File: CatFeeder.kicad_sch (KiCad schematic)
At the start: 54 parts, among them J1 B2B-XH-A(LF)(SN), J10 B2B-XH-A(LF)(SN), J11 B2B-XH-A(LF)(SN), J12 B2B-XH-A(LF)(SN), J13 B2B-XH-A(LF)(SN), J2 B2B-XH-A(LF)(SN), J3 B3B-XH-A(LF)(SN), J4 Barrel_Jack, J5 B4B-XH-A(LF)(SN), J6 Conn_01x08_Female, J7 Conn_01x08_Female, J8 B2B-XH-A(LF)(SN), J9 B2B-XH-A(LF)(SN), Q1 Q_NPN_BEC, Q2 Q_NPN_BEC, U1 SN74LVC1T45DBV, U2 LM2586SX-ADJ/NOPB_1, U3 DRV8871DDA

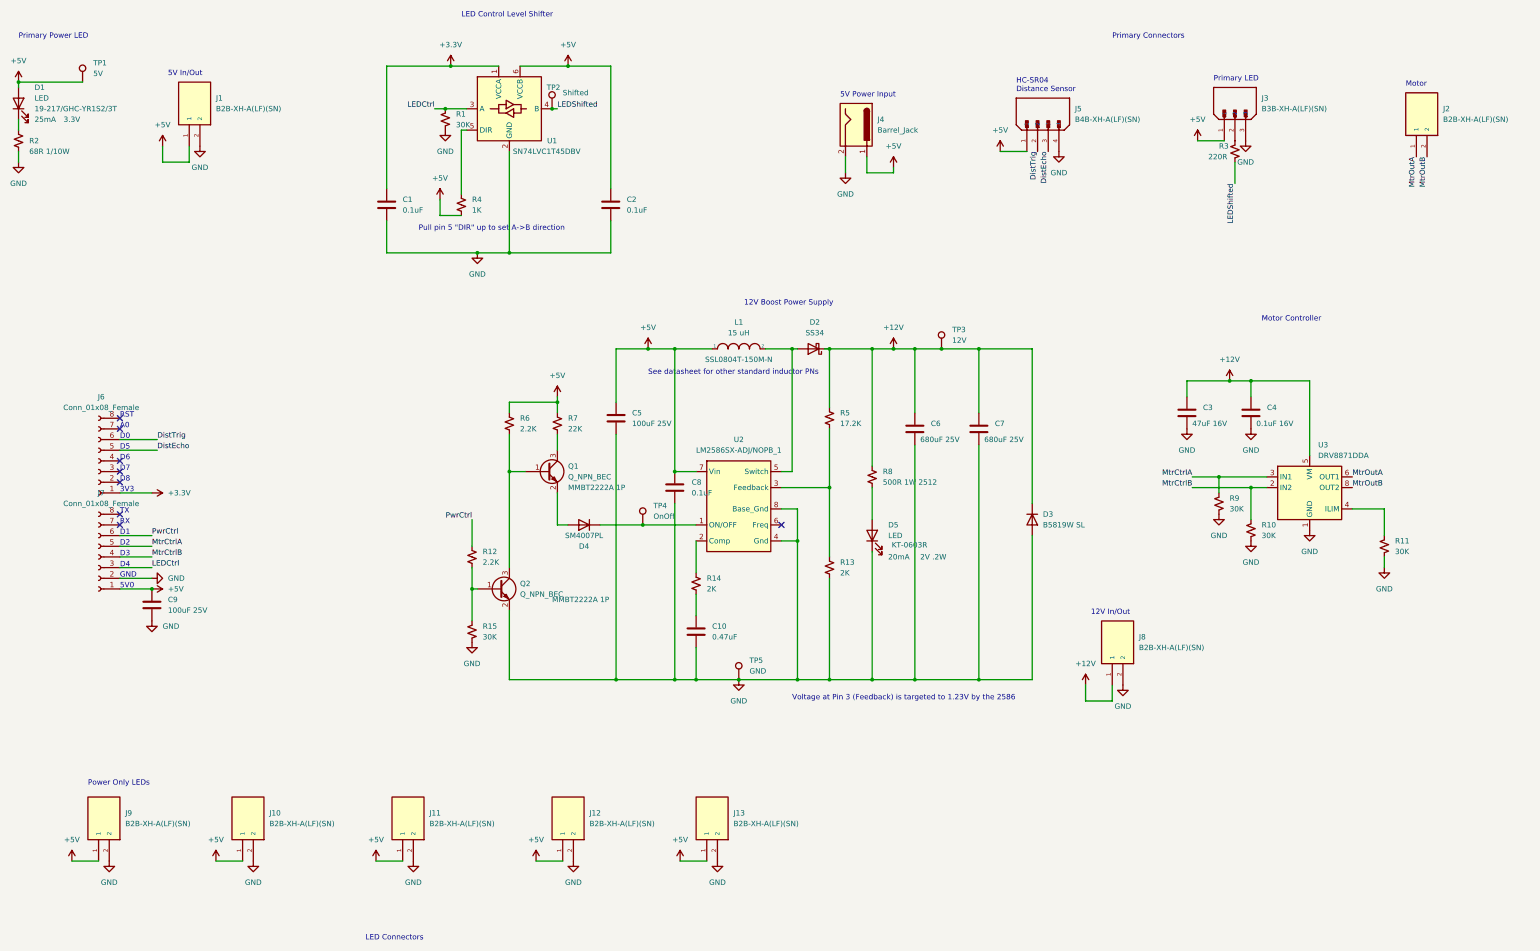
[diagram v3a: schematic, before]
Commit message: rounded corners, added polarity silkscreen, dimmed the main power LED, fixed polarized cap schematic symbols.
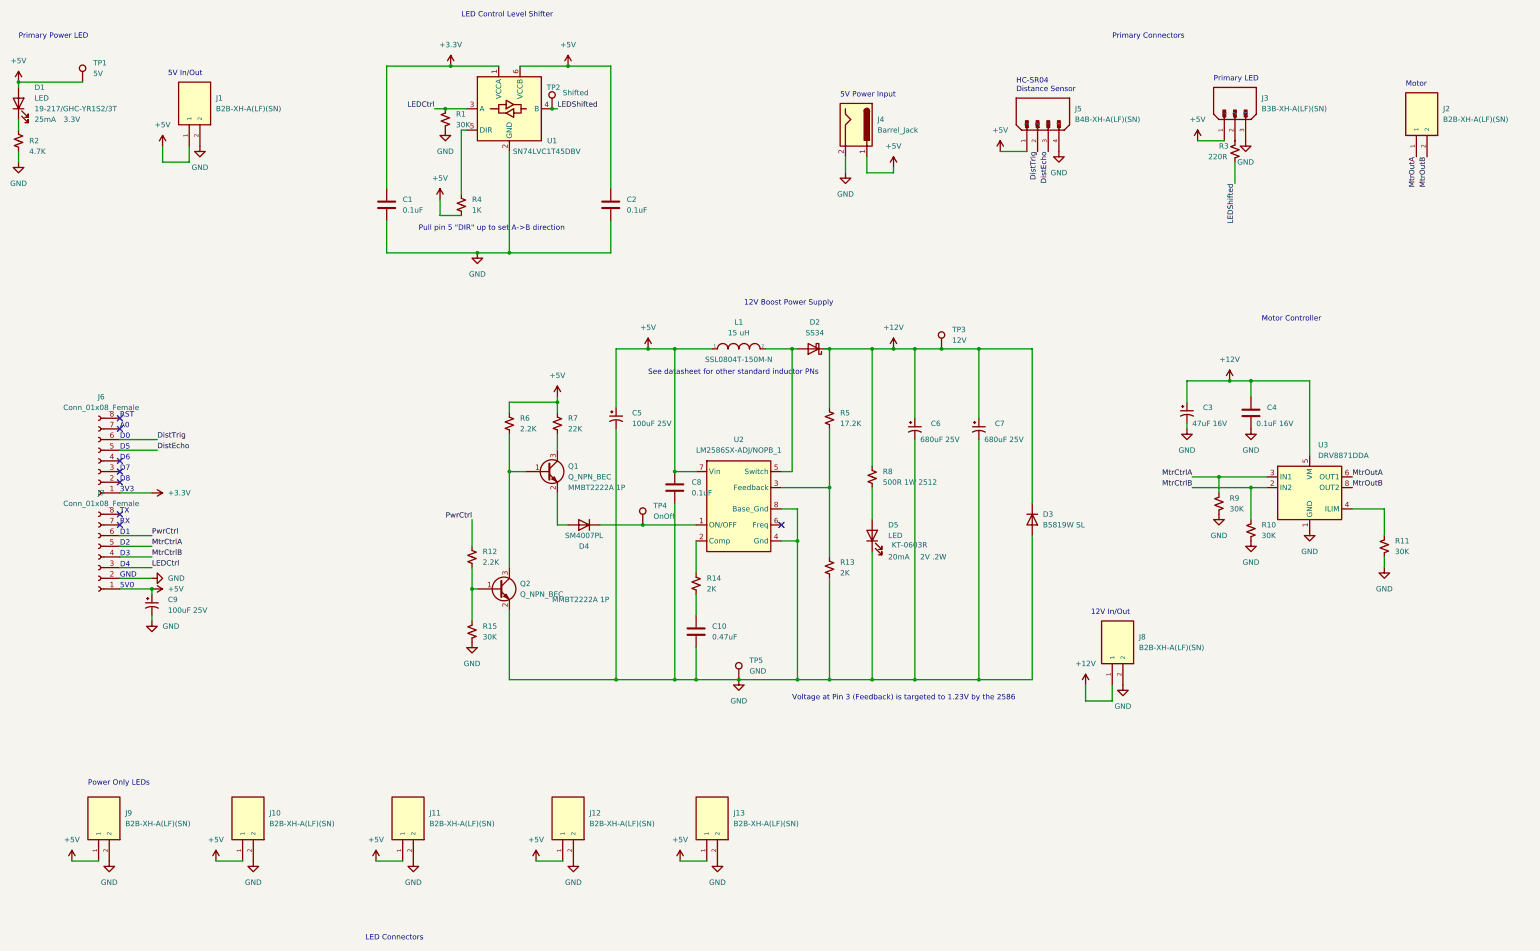
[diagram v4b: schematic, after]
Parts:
- C3, C5, C6, C7, C9: symbol Device:C -> Device:C_Polarized_Small_US
- R2: value 68R 1/10W -> 4.7K; footprint Resistor_SMD:R_0603_1608Metric -> Resistor_SMD:R_0805_2012Metric; PN 0603WAF680JT5E -> 0805W8F4701T5E
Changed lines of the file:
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@@
   (junction (at 233.68 102.87) (diameter 0) (color 0 0 0 0)
   )
+  (junction (at 72.39 160.02) (diameter 0) (color 0 0 0 0)
+  )
   (junction (at 189.23 144.78) (diameter 0) (color 0 0 0 0)
   )
@@
   (junction (at 212.09 181.61) (diameter 0) (color 0 0 0 0)
   )
-  (junction (at 72.39 160.02) (diameter 0) (color 0 0 0 0)
-  )
   (junction (at 233.68 181.61) (diameter 0) (color 0 0 0 0)
   )
@@
     (stroke (width 0) (type default) (color 0 0 0 0))
   )
-  (wire (pts (xy 254 125.73) (xy 254 181.61))
+  (wire (pts (xy 254 124.46) (xy 254 181.61))
     (stroke (width 0) (type default) (color 0 0 0 0))
   )
@@
     (stroke (width 0) (type default) (color 0 0 0 0))
   )
-  (wire (pts (xy 182.88 123.19) (xy 182.88 181.61))
+  (wire (pts (xy 182.88 121.92) (xy 182.88 181.61))
     (stroke (width 0) (type default) (color 0 0 0 0))
   )
@@
     (stroke (width 0) (type default) (color 0 0 0 0))
   )
-  (wire (pts (xy 269.24 125.73) (xy 269.24 181.61))
+  (wire (pts (xy 269.24 124.46) (xy 269.24 181.61))
     (stroke (width 0) (type default) (color 0 0 0 0))
   )
@@
     (stroke (width 0) (type default) (color 0 0 0 0))
   )
-  (wire (pts (xy 318.77 110.49) (xy 318.77 114.3))
+  (wire (pts (xy 318.77 110.49) (xy 318.77 115.57))
     (stroke (width 0) (type default) (color 0 0 0 0))
   )
@@
     (stroke (width 0) (type default) (color 0 0 0 0))
   )
-  (wire (pts (xy 182.88 102.87) (xy 182.88 115.57))
+  (wire (pts (xy 182.88 102.87) (xy 182.88 116.84))
     (stroke (width 0) (type default) (color 0 0 0 0))
   )
@@
     (stroke (width 0) (type default) (color 0 0 0 0))
   )
-  (wire (pts (xy 254 118.11) (xy 254 102.87))
+  (wire (pts (xy 254 102.87) (xy 254 119.38))
     (stroke (width 0) (type default) (color 0 0 0 0))
   )
@@
     (stroke (width 0) (type default) (color 0 0 0 0))
   )
-  (wire (pts (xy 269.24 118.11) (xy 269.24 102.87))
+  (wire (pts (xy 269.24 102.87) (xy 269.24 119.38))
     (stroke (width 0) (type default) (color 0 0 0 0))
   )
@@
     (stroke (width 0) (type default) (color 0 0 0 0))
   )
+  (wire (pts (xy 72.39 160.02) (xy 72.39 161.29))
+    (stroke (width 0) (type default) (color 0 0 0 0))
+  )
   (wire (pts (xy 198.12 224.79) (xy 204.47 224.79))
     (stroke (width 0) (type default) (color 0 0 0 0))
@@
     (stroke (width 0) (type default) (color 0 0 0 0))
   )
+  (wire (pts (xy 72.39 166.37) (xy 72.39 167.64))
+    (stroke (width 0) (type default) (color 0 0 0 0))
+  )
   (wire (pts (xy 128.27 35.56) (xy 128.27 64.77))
     (stroke (width 0) (type default) (color 0 0 0 0))
@@
     (stroke (width 0) (type default) (color 0 0 0 0))
   )
+  (wire (pts (xy 318.77 120.65) (xy 318.77 121.92))
+    (stroke (width 0) (type default) (color 0 0 0 0))
+  )
   (wire (pts (xy 157.48 80.01) (xy 181.61 80.01))
     (stroke (width 0) (type default) (color 0 0 0 0))
@@
     (pin "6")
   )
-  (symbol (lib_id "Device:C") (at 72.39 163.83 0) (unit 1)
+  (symbol (lib_id "Device:C_Polarized_Small_US") (at 72.39 163.83 0) (unit 1)
     (in_bom yes) (on_board yes) (fields_autoplaced)
     (property "Reference" "C9" (id 0) (at 76.2 162.5599 0)
@@
       (effects (font (size 1.27 1.27)) (justify left))
     )
-    (property "Footprint" "Capacitor_THT:CP_Radial_D8.0mm_P3.50mm" (id 2) (at 73.3552 167.64 0)
+    (property "Footprint" "Capacitor_THT:CP_Radial_D8.0mm_P3.50mm" (id 2) (at 72.39 163.83 0)
       (effects (font (size 1.27 1.27)) hide)
     )
@@
     (pin "2")
   )
-  (symbol (lib_id "Device:C") (at 182.88 119.38 0) (unit 1)
+  (symbol (lib_id "Device:C_Polarized_Small_US") (at 182.88 119.38 0) (unit 1)
     (in_bom yes) (on_board yes) (fields_autoplaced)
     (property "Reference" "C5" (id 0) (at 186.69 118.1099 0)
@@
       (effects (font (size 1.27 1.27)) (justify left))
     )
-    (property "Footprint" "Capacitor_THT:CP_Radial_D8.0mm_P3.50mm" (id 2) (at 183.8452 123.19 0)
+    (property "Footprint" "Capacitor_THT:CP_Radial_D8.0mm_P3.50mm" (id 2) (at 182.88 119.38 0)
       (effects (font (size 1.27 1.27)) hide)
     )
@@
     (pin "1")
   )
-  (symbol (lib_id "Device:C") (at 318.77 118.11 0) (unit 1)
+  (symbol (lib_id "Device:C_Polarized_Small_US") (at 318.77 118.11 0) (unit 1)
     (in_bom yes) (on_board yes)
     (property "Reference" "C3" (id 0) (at 322.58 116.8399 0)
@@
       (effects (font (size 1.27 1.27)) (justify left))
     )
-    (property "Footprint" "Capacitor_SMD:CP_Elec_5x5.4" (id 2) (at 319.7352 121.92 0)
+    (property "Footprint" "Capacitor_SMD:CP_Elec_5x5.4" (id 2) (at 318.77 118.11 0)
       (effects (font (size 1.27 1.27)) hide)
     )
@@
     (pin "1")
   )
-  (symbol (lib_id "Device:C") (at 269.24 121.92 0) (unit 1)
+  (symbol (lib_id "Device:C_Polarized_Small_US") (at 269.24 121.92 0) (unit 1)
     (in_bom yes) (on_board yes)
     (property "Reference" "C7" (id 0) (at 273.05 120.6499 0)
@@
       (effects (font (size 1.27 1.27)) (justify left))
     )
-    (property "Footprint" "Capacitor_THT:CP_Radial_D8.0mm_P3.50mm" (id 2) (at 270.2052 125.73 0)
+    (property "Footprint" "Capacitor_THT:CP_Radial_D8.0mm_P3.50mm" (id 2) (at 269.24 121.92 0)
       (effects (font (size 1.27 1.27)) hide)
     )
@@
       (effects (font (size 1.27 1.27)) (justify left))
     )
-    (property "Value" "68R 1/10W" (id 1) (at 43.18 55.88 0)
+    (property "Value" "4.7K" (id 1) (at 43.18 55.88 0)
       (effects (font (size 1.27 1.27)) (justify left))
     )
-    (property "Footprint" "Resistor_SMD:R_0603_1608Metric" (id 2) (at 40.64 53.34 0)
+    (property "Footprint" "Resistor_SMD:R_0805_2012Metric" (id 2) (at 40.64 53.34 0)
       (effects (font (size 1.27 1.27)) hide)
     )
@@
       (effects (font (size 1.27 1.27)) hide)
     )
-    (property "PN" "0603WAF680JT5E" (id 4) (at 40.64 53.34 0)
+    (property "PN" "0805W8F4701T5E" (id 4) (at 40.64 53.34 0)
       (effects (font (size 1.27 1.27)) hide)
     )
@@
     (pin "1")
   )
-  (symbol (lib_id "Device:C") (at 254 121.92 0) (unit 1)
+  (symbol (lib_id "Device:C_Polarized_Small_US") (at 254 121.92 0) (unit 1)
     (in_bom yes) (on_board yes)
     (property "Reference" "C6" (id 0) (at 257.81 120.6499 0)
@@
       (effects (font (size 1.27 1.27)) (justify left))
     )
-    (property "Footprint" "Capacitor_THT:CP_Radial_D8.0mm_P3.50mm" (id 2) (at 254.9652 125.73 0)
+    (property "Footprint" "Capacitor_THT:CP_Radial_D8.0mm_P3.50mm" (id 2) (at 254 121.92 0)
       (effects (font (size 1.27 1.27)) hide)
     )
@@
     )
     (path "/e897f7f8-beee-4997-916a-562d1390e838"
-      (reference "R2") (unit 1) (value "68R 1/10W") (footprint "Resistor_SMD:R_0603_1608Metric")
+      (reference "R2") (unit 1) (value "4.7K") (footprint "Resistor_SMD:R_0805_2012Metric")
     )
     (path "/8c95ae70-46a7-4c87-9b1c-d0a941a7d9f1"

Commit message: Manufacturing outputs
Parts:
- J6, J7: PN (none) -> C27438
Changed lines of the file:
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@@
+      (effects (font (size 1.27 1.27)) hide)
+    )
+    (property "PN" "C27438" (id 4) (at 59.69 129.54 0)
       (effects (font (size 1.27 1.27)) hide)
     )
@@
       (effects (font (size 1.27 1.27)) hide)
     )
+    (property "PN" "C27438" (id 4) (at 59.69 152.4 0)
+      (effects (font (size 1.27 1.27)) hide)
+    )
